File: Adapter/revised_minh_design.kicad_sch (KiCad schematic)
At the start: 15 parts, among them J2 Conn_02x08_Odd_Even, J3 Conn_02x08_Odd_Even, J4 Conn_02x08_Odd_Even, J5 Conn_01x02_Male, U1 ESP32-DevKit-C, U6 MCP3464R, U7 MCP3464R, U8 DAC8568IAPW

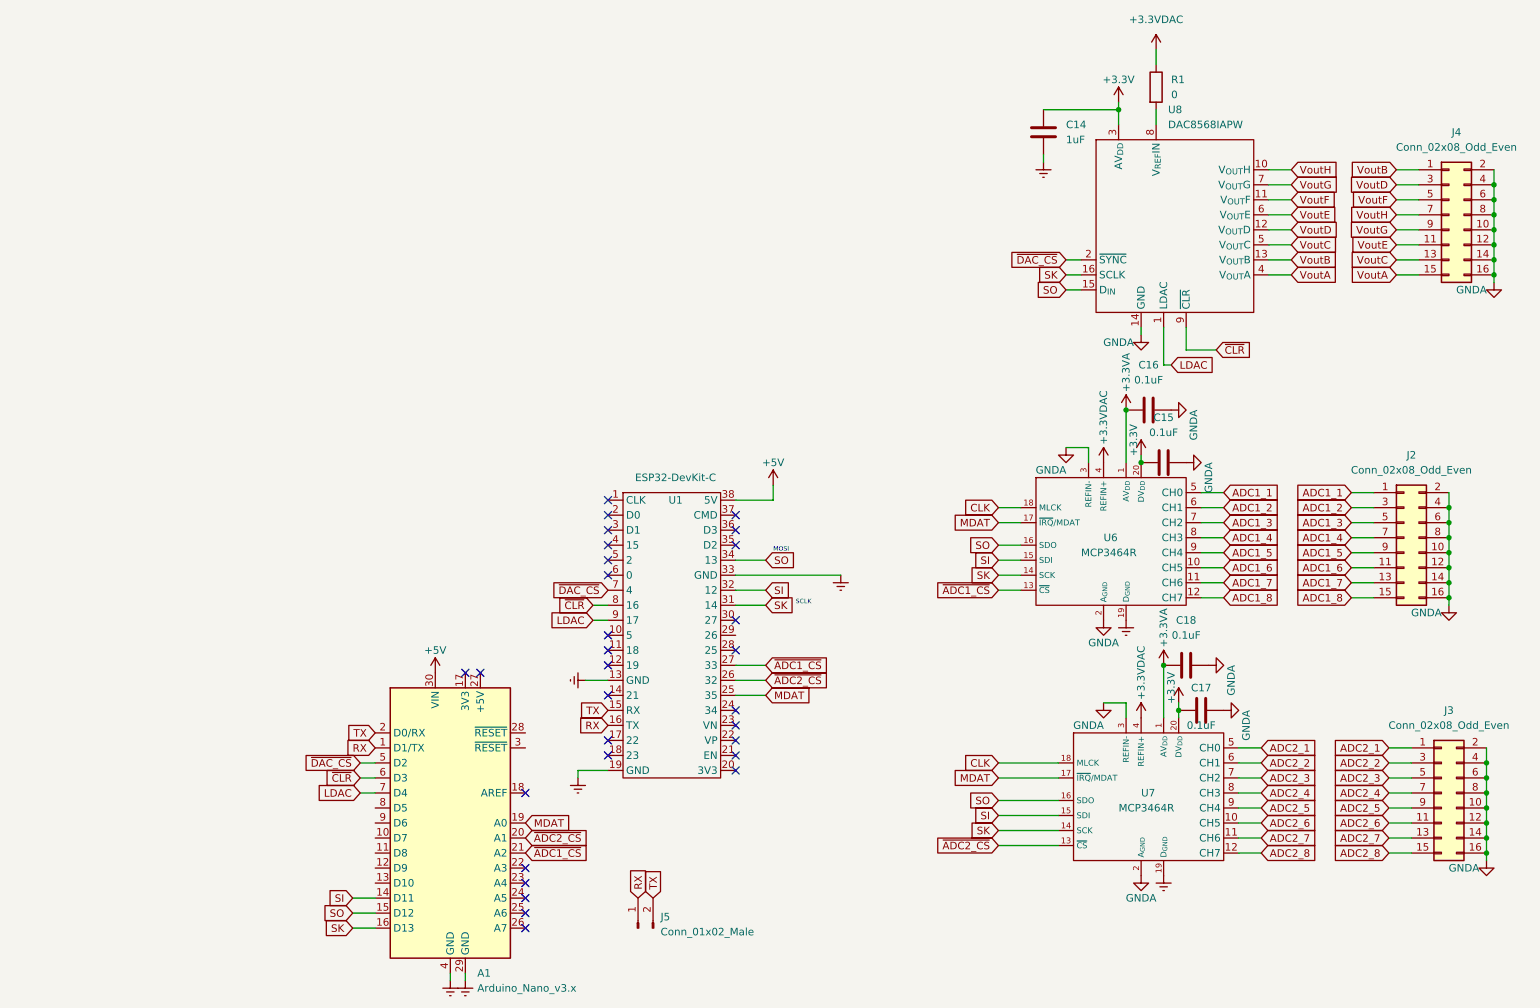
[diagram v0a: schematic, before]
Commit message: adapter board 4 layers
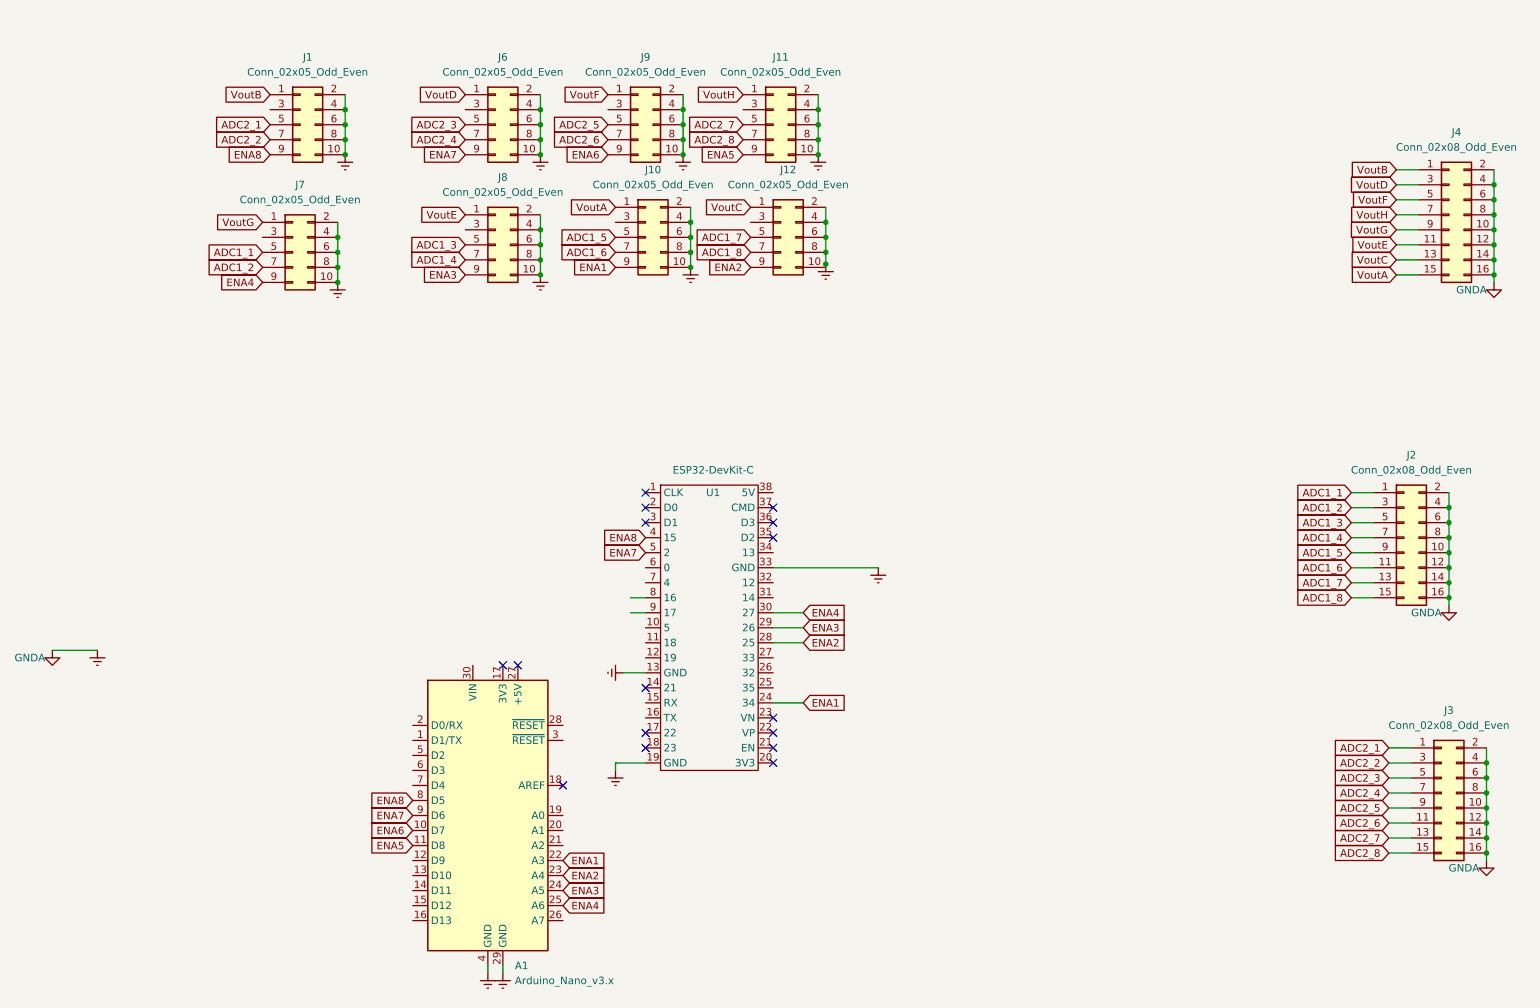
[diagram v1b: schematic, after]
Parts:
- removed C14: 1uF, Capacitor_SMD:C_0805_2012Metric_Pad1.18x1.45mm_HandSolder, symbol Device:C
- removed C15, C16, C17, C18: 0.1uF, Capacitor_SMD:C_0805_2012Metric_Pad1.18x1.45mm_HandSolder, symbol Device:C
- removed J5: Conn_01x02_Male, Connector_PinSocket_2.54mm:PinSocket_1x02_P2.54mm_Vertical, symbol Connector:Conn_01x02_Male
- removed R1: 0, Resistor_SMD:R_0805_2012Metric_Pad1.20x1.40mm_HandSolder, symbol Device:R
- removed U6, U7: MCP3464R, Package_SO:TSSOP-20_4.4x6.5mm_P0.65mm, symbol design:MCP3464R
- removed U8: DAC8568IAPW, Package_SO:TSSOP-16-1EP_4.4x5mm_P0.65mm, symbol design:DAC8568IAPW
- added J1, J10, J11, J12, J6, J7, J8, J9: Conn_02x05_Odd_Even, Connector_PinSocket_2.54mm:PinSocket_2x05_P2.54mm_Vertical, symbol Connector_Generic:Conn_02x05_Odd_Even
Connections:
- net GNDA is gone; now on net Earth: J2.10 (Pin_10), J2.12 (Pin_12), J2.14 (Pin_14), J2.16 (Pin_16), J2.2 (Pin_2), J2.4 (Pin_4), J2.6 (Pin_6), J2.8 (Pin_8), J3.10 (Pin_10), J3.12 (Pin_12), J3.14 (Pin_14), J3.16 (Pin_16), J3.2 (Pin_2), J3.4 (Pin_4), J3.6 (Pin_6), J3.8 (Pin_8), J4.10 (Pin_10), J4.12 (Pin_12), J4.14 (Pin_14), J4.16 (Pin_16), J4.2 (Pin_2), J4.4 (Pin_4), J4.6 (Pin_6), J4.8 (Pin_8)
- net ADC1_1: now also J7.5 (Pin_5)
- net ADC1_2: now also J7.7 (Pin_7)
- net ADC1_3: now also J8.5 (Pin_5)
- net ADC1_4: now also J8.7 (Pin_7)
- net ADC1_5: now also J10.5 (Pin_5)
- net ADC1_6: now also J10.7 (Pin_7)
- net ADC1_7: now also J12.5 (Pin_5)
- net ADC1_8: now also J12.7 (Pin_7)
- net ADC2_1: now also J1.5 (Pin_5)
- net ADC2_2: now also J1.7 (Pin_7)
- net ADC2_3: now also J6.5 (Pin_5)
- net ADC2_4: now also J6.7 (Pin_7)
- net ADC2_5: now also J9.5 (Pin_5)
- net ADC2_6: now also J9.7 (Pin_7)
- net ADC2_7: now also J11.5 (Pin_5)
- net ADC2_8: now also J11.7 (Pin_7)
- net Earth: now also J1.10 (Pin_10), J1.2 (Pin_2), J1.4 (Pin_4), J1.6 (Pin_6), J1.8 (Pin_8), J10.10 (Pin_10), J10.2 (Pin_2), J10.4 (Pin_4), J10.6 (Pin_6), J10.8 (Pin_8), J11.10 (Pin_10), J11.2 (Pin_2), J11.4 (Pin_4), J11.6 (Pin_6), J11.8 (Pin_8), J12.10 (Pin_10), J12.2 (Pin_2), J12.4 (Pin_4), J12.6 (Pin_6), J12.8 (Pin_8), J6.10 (Pin_10), J6.2 (Pin_2), J6.4 (Pin_4), J6.6 (Pin_6), J6.8 (Pin_8), J7.10 (Pin_10), J7.2 (Pin_2), J7.4 (Pin_4), J7.6 (Pin_6), J7.8 (Pin_8), J8.10 (Pin_10), J8.2 (Pin_2), J8.4 (Pin_4), J8.6 (Pin_6), J8.8 (Pin_8), J9.10 (Pin_10), J9.2 (Pin_2), J9.4 (Pin_4), J9.6 (Pin_6), J9.8 (Pin_8)
- net VoutA: now also J10.1 (Pin_1)
- net VoutB: now also J1.1 (Pin_1)
- net VoutC: now also J12.1 (Pin_1)
- net VoutD: now also J6.1 (Pin_1)
- net VoutE: now also J8.1 (Pin_1)
- net VoutF: now also J9.1 (Pin_1)
- net VoutG: now also J7.1 (Pin_1)
- net VoutH: now also J11.1 (Pin_1)
- net ENA6: now reaches A1.10 (D7)
- net ENA6: now also J9.9 (Pin_9)
- net ENA5: now reaches A1.11 (D8)
- net ENA5: now also J11.9 (Pin_9)
- net ENA1: now reaches A1.22 (A3)
- net ENA1: now also U1.24 (34), J10.9 (Pin_9)
- net ENA2: now reaches A1.23 (A4)
- net ENA2: now also U1.28 (25), J12.9 (Pin_9)
- net ENA3: now reaches A1.24 (A5)
- net ENA3: now also U1.29 (26), J8.9 (Pin_9)
- net ENA4: now reaches A1.25 (A6)
- net ENA4: now also U1.30 (27), J7.9 (Pin_9)
- net ENA8: now reaches A1.8 (D5)
- net ENA8: now also U1.4 (15), J1.9 (Pin_9)
- net ENA7: now reaches A1.9 (D6)
- net ENA7: now also U1.5 (2), J6.9 (Pin_9)
- net +5V: no longer names the net of A1.30 (VIN)
- net +5V: no longer U1.38 (5V)
- net LDAC: no longer names the net of A1.7 (D4)
- net LDAC: no longer U1.9 (17)
- net MDAT: no longer names the net of A1.19 (A0)
- net MDAT: no longer U1.25 (35)
- net RX: no longer names the net of A1.1 (D1/TX)
- net RX: no longer U1.16 (TX)
- net SI: no longer names the net of A1.14 (D11)
- net SI: no longer U1.32 (12)
- net SK: no longer names the net of A1.16 (D13)
- net SK: no longer U1.31 (14)
- net SO: no longer names the net of A1.15 (D12)
- net SO: no longer U1.34 (13)
- net TX: no longer names the net of A1.2 (D0/RX)
- net TX: no longer U1.15 (RX)
- net ~{ADC1_CS}: no longer names the net of A1.21 (A2)
- net ~{ADC1_CS}: no longer U1.27 (33)
- net ~{ADC2_CS}: no longer names the net of A1.20 (A1)
- net ~{ADC2_CS}: no longer U1.26 (32)
- net ~{CLR}: no longer names the net of A1.6 (D3)
- net ~{CLR}: no longer U1.8 (16)
- net ~{DAC_CS}: no longer names the net of A1.5 (D2)
- net ~{DAC_CS}: no longer U1.7 (4)
- no-connect marks 30 -> 16
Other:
- note removed: "MOSI"
- note removed: "SCLK"
- moved on the sheet: A1, U1
